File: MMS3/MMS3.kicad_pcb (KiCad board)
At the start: 2 copper layers, 100 x 50 mm, 162 parts, among them J1 86093488324755V1LF, J1 Chainbus in, J2 AMASS XT60, J2 Chainbus Out, J3 Programming header, J7 AMASS XT60, J8 RJ45_LED_Shielded, J800 USB_C_Receptacle_USB2.0_16P, J9 RJ45_LED_Shielded, Q700 MMST3904, SW1 BOOT, SW2 RESET, U1 STM32F405RGTx, U302 CH334P, U4 TPD2EUSB30DRTR-TP, U401 TPD2EUSB30DRTR-TP, U5 TPD2EUSB30DRTR-TP, U500 TJA1044GTK_3Z, U501 TJA1044GTK_3Z, U6 AT24C256C, U700 STM32F103CBTx, U801 FSUSB42UMX, U802 FSUSB42UMX, X1 X32258MOB4SI, X2 Q13FC1350000400, Y700 Crystal_GND24, Y900 Crystal_GND24

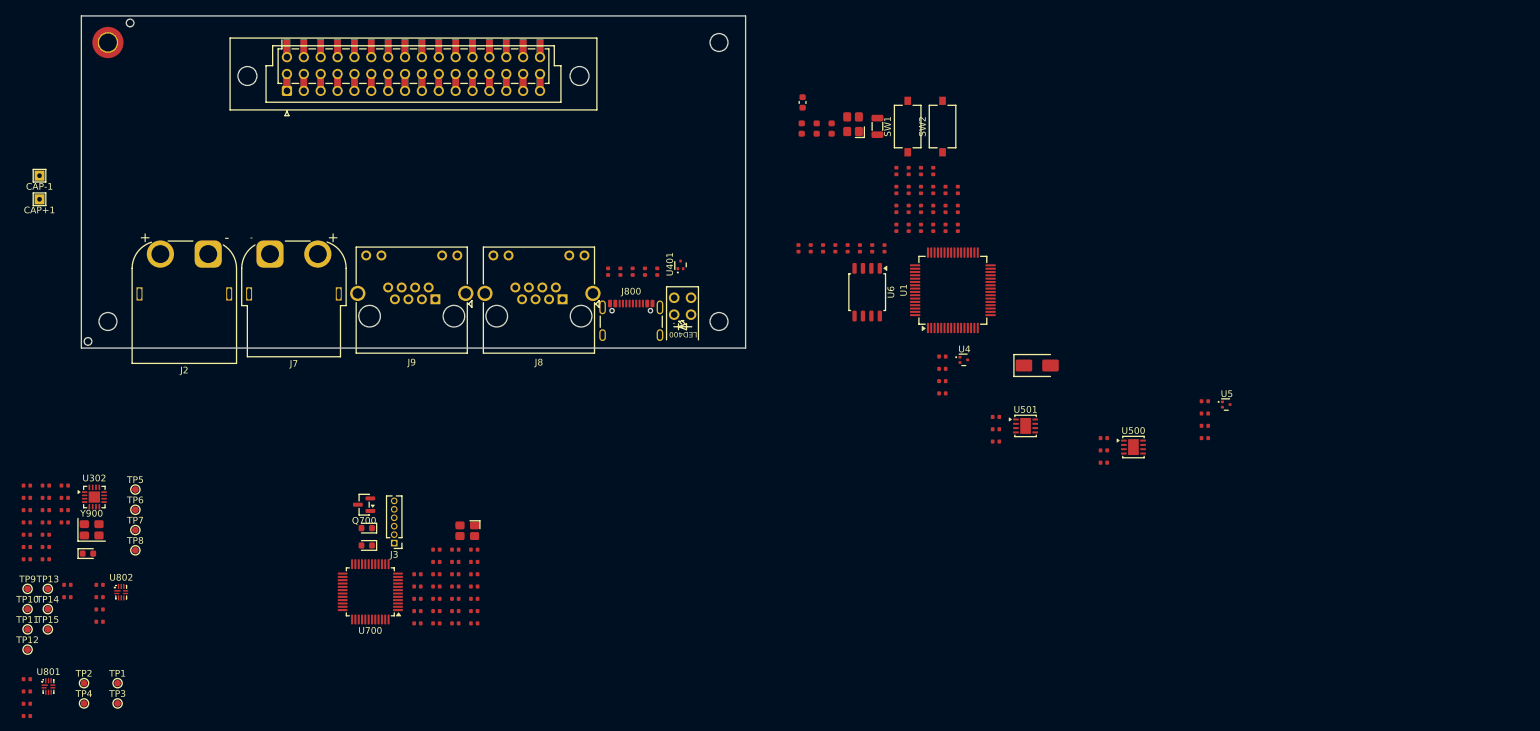
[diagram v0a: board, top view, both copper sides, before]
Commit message: schematic + partly layout
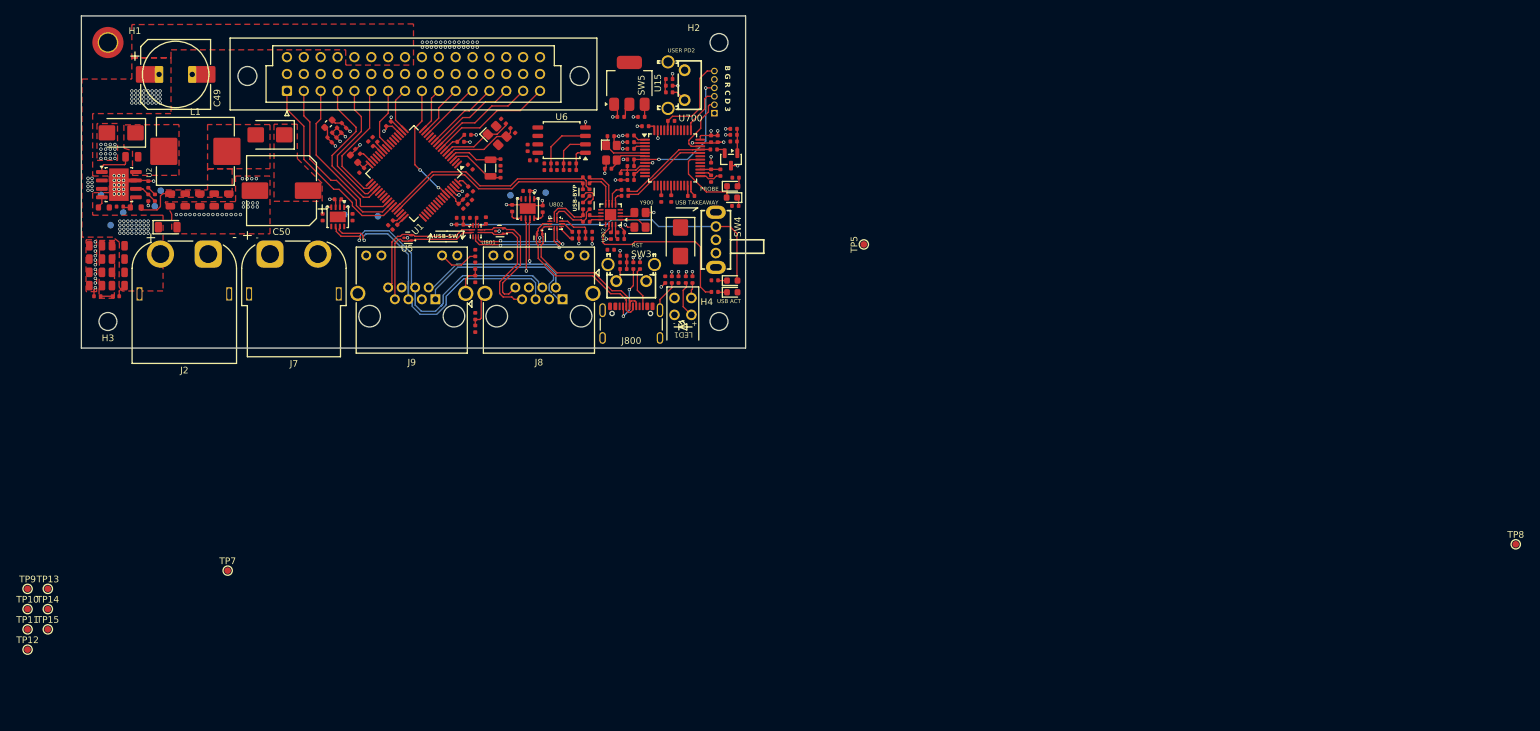
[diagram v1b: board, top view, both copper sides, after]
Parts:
- removed C14: 10uF, PCM_JLCPCB:C_0603
- removed C707, C708: 33pF, PCM_JLCPCB:C_0402
- removed CAP+1: Capacitor +, TestPoint:TestPoint_THTPad_1.5x1.5mm_Drill0.7mm
- removed CAP-1: Capacitor -, TestPoint:TestPoint_THTPad_1.5x1.5mm_Drill0.7mm
- removed H7, H9: ~, PCM_JLCPCB:Hole_Tooling_JLCPCB
- removed the J1 at (149.0, 89.5)
- removed the J2 at (149.0, 89.6)
- removed LED400: FixLed307, FixLed307:FixLed307
- removed R32: 22Ω, PCM_JLCPCB:R_0402
- removed SW1: BOOT, Button_Switch_SMD:SW_Tactile_SPST_NO_Straight_CK_PTS636Sx25SMTRLFS
- removed SW2: RESET, Button_Switch_SMD:SW_Tactile_SPST_NO_Straight_CK_PTS636Sx25SMTRLFS
- removed TP6: TestPoint, TestPoint:TestPoint_Pad_D1.0mm
- added C30: 10uF, PCM_JLCPCB:C_0805, F.Cu at (104.5, 118.6)
- added C31: 10uF, PCM_JLCPCB:C_0805, F.Cu at (101.2, 120.6)
- added C32: 10uF, PCM_JLCPCB:C_0805, F.Cu at (104.5, 120.6)
- added C33: 10uF, PCM_JLCPCB:C_0805, F.Cu at (101.2, 122.6)
- added C34: 10uF, PCM_JLCPCB:C_0805, F.Cu at (104.5, 122.6)
- added C35: 10uF, PCM_JLCPCB:C_0805, F.Cu at (101.2, 116.6)
- added C36: 10uF, PCM_JLCPCB:C_0402, F.Cu at (137.8, 98.5)
- added C37: 10uF, PCM_JLCPCB:C_0402, F.Cu at (137.1, 100.7)
- added C38: 220nF, PCM_JLCPCB:C_0805, F.Cu at (104.5, 116.6)
- added C39: 220nF, PCM_JLCPCB:C_0805, F.Cu at (101.2, 118.6)
- added C40: 100nF, PCM_JLCPCB:C_0805, F.Cu at (106.6, 103.2)
- added C41: 22uF, PCM_JLCPCB:C_0805, F.Cu at (112.4, 109.7)
- added C42: 22uF, PCM_JLCPCB:C_0805, F.Cu at (119.0, 109.7)
- added C43: 47pF, PCM_JLCPCB:C_0402, F.Cu at (109.1, 109.4)
- added C44: 4.7nF, PCM_JLCPCB:C_0402, F.Cu at (109.1, 107.4)
- added C45: 22uF, PCM_JLCPCB:C_0805, F.Cu at (116.8, 109.7)
- added C46: 22uF, PCM_JLCPCB:C_0805, F.Cu at (114.6, 109.7)
- added C47: 22uF, PCM_JLCPCB:C_0805, F.Cu at (121.2, 109.7)
- added C49: 100uF, Capacitor_SMD:CP_Elec_10x10, F.Cu at (113.2, 90.8)
- added C50: 100uF, Capacitor_SMD:CP_Elec_10x10, F.Cu at (129.1, 108.3)
- added C69: 100nF, PCM_JLCPCB:C_0402, F.Cu at (180.2, 97.2)
- added C74: 100nF, PCM_JLCPCB:C_0402, F.Cu at (183.3, 97.2)
- added D1: SMF58CA, PCM_JLCPCB:D_SOD-123FL, F.Cu at (112.0, 113.8)
- added D3: SS510B, PCM_JLCPCB:D_SMB, F.Cu at (105.0, 99.6)
- added D4: SS510B, PCM_JLCPCB:D_SMB, F.Cu at (127.4, 99.9)
- added D5: SS510B, PCM_JLCPCB:D_SMB, F.Cu at (189.2, 116.0)
- added L1: YSPI1050-100M, Inductor_SMD:L_Sunlord_MWSA1005S, F.Cu at (116.2, 102.4)
- added LED1: FixLed307, FixLed307:FixLed307, F.Cu at (189.5, 127.0)
- added R33: 24.9kΩ, PCM_JLCPCB:R_0402, F.Cu at (104.2, 124.2)
- added R34: 24.9kΩ, PCM_JLCPCB:R_0402, F.Cu at (101.4, 124.2)
- added R36: 43kΩ, PCM_JLCPCB:R_0603, F.Cu at (107.2, 110.8)
- added R37: 8.2kΩ, PCM_JLCPCB:R_0402, F.Cu at (104.8, 110.7)
- added R38: 12kΩ, PCM_JLCPCB:R_0402, F.Cu at (110.1, 109.4)
- added R39: 240kΩ, PCM_JLCPCB:R_0603, F.Cu at (102.4, 110.8)
- added R40: 1kΩ, PCM_JLCPCB:R_0402, F.Cu at (190.0, 121.7)
- added SW3: TC-6615Z-12.5-260, Tact-sw:SW-TH_4P-L7.3-TC-6615Z-12.5-260, F.Cu at (181.8, 120.7)
- added SW4: SK12D07VG5, Slide-SW:SW-TH_SK12D07VG5-1, F.Cu at (194.5, 115.7)
- added SW5: TC-6615Z-12.5-260, Tact-sw:SW-TH_4P-L7.3-TC-6615Z-12.5-260, F.Cu at (188.6, 92.4)
- added TP16: TestPoint, TestPoint:TestPoint_Pad_D1.0mm, B.Cu at (103.4, 113.5)
- added TP17: TestPoint, TestPoint:TestPoint_Pad_D1.0mm, B.Cu at (110.0, 110.7)
- added TP18: TestPoint, TestPoint:TestPoint_Pad_D1.0mm, B.Cu at (105.3, 111.6)
- added TP19: TestPoint, TestPoint:TestPoint_Pad_D1.0mm, B.Cu at (111.0, 108.3)
- added TP20: TestPoint, TestPoint:TestPoint_Pad_D1.0mm, B.Cu at (102.0, 109.0)
- added U15: AMS1117-3.3, Package_TO_SOT_SMD:SOT-223-3_TabPin2, F.Cu at (181.5, 92.2)
- added U2: TPS54560BDDA, Package_SO:Texas_R-PDSO-G8_EP2.95x4.9mm_Mask2.4x3.1mm_ThermalVias, F.Cu at (104.7, 107.4)
- C12: value 10uF -> 100nF; footprint PCM_JLCPCB:C_0603 -> PCM_JLCPCB:C_0402
- D6: value SS34 -> Red; footprint PCM_JLCPCB:D_SMA -> PCM_JLCPCB:D_0603
- J3, TP1, TP2, TP3, TP4: moved to B.Cu
- R22: value 22Ω -> 100Ω
- R27, R31: value 22Ω -> 1kΩ
- moved TP8 207.8 mm to (314.9, 161.5)
- moved R4 132.6 mm to (142.5, 101.2), turned to -45 degrees
- moved U5 125.8 mm to (148.1, 115.4), turned to 180 degrees
- moved TP5 115.7 mm to (216.8, 116.4), turned to 90 degrees
- moved R6 112.9 mm to (158.3, 119.6), turned to 90 degrees
- moved R2 112.5 mm to (158.3, 117.7), turned to 90 degrees
- moved C2 111.4 mm to (158.3, 121.6), turned to -90 degrees
- moved R308 108.4 mm to (194.3, 123.5)
- moved U501 108.2 mm to (137.6, 112.2), turned to -90 degrees
- moved R31 107.7 mm to (194.3, 121.8), turned to 180 degrees
- moved C28 106.1 mm to (178.7, 100.1)
- moved C4 105.7 mm to (135.3, 112.3), turned to 90 degrees
- moved C6 104.9 mm to (137.6, 109.6), turned to 180 degrees
- moved D301 104.7 mm to (197.0, 123.6)
- moved R27 104.0 mm to (191.0, 121.7), turned to -90 degrees
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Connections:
- net Net-(R18-Pad1) renamed /USB HUB/USBBYP.D+
- C12 pad 1: +3V3 -> Net-(U1-NRST)
- D6 pad 1: +5V -> Net-(D6-Pad1)
- D6 pad 2: VBUS -> /Slide-SW/SEL
- J1 pad a1: (no net) -> /Interboard_connector/Altmode3
- J1 pad a10: (no net) -> /Interboard_connector/Altmode9
- J1 pad a11: (no net) -> /Interboard_connector/Altmode8
- J1 pad a12: (no net) -> /Interboard_connector/Altmode7
- J1 pad a13: (no net) -> /Interboard_connector/Altmode15
- J1 pad a14: (no net) -> /Interboard_connector/Altmode14
- J1 pad a15: (no net) -> /Interboard_connector/Altmode13
- J1 pad a16: (no net) -> /Interboard_connector/Altmode12
- J1 pad a2: (no net) -> /Interboard_connector/Altmode2
- J1 pad a3: (no net) -> /Interboard_connector/Altmode1
- J1 pad a4: (no net) -> /Interboard_connector/Altmode6
- J1 pad a5: (no net) -> /Interboard_connector/Altmode5
- J1 pad a6: (no net) -> /Interboard_connector/Altmode4
- J1 pad a7: (no net) -> /Interboard_connector/Altmode16
- J1 pad a8: (no net) -> /Interboard_connector/Altmode10
- J1 pad a9: (no net) -> /Interboard_connector/Altmode11
- J1 pad b1: (no net) -> /Interboard_connector/Chainbus_UART_addr0
- J1 pad b10: (no net) -> /I2C_Flash/I2C_Memory.SCL
- J1 pad b11: (no net) -> /Interboard_connector/Chainbus_I2C_addr2
- J1 pad b12: (no net) -> /Interboard_connector/Chainbus.SCK
- J1 pad b13: (no net) -> /Interboard_connector/Chainbus.MOSI
- J1 pad b14: (no net) -> /Interboard_connector/Chainbus.MISO
- J1 pad b15: (no net) -> /Interboard_connector/Chainbus.RX
- J1 pad b16: (no net) -> /Interboard_connector/Chainbus.TX
- J1 pad b2: (no net) -> /Interboard_connector/Chainbus_UART_addr1
- J1 pad b3: (no net) -> /Interboard_connector/Chainbus_UART_addr2
- J1 pad b4: (no net) -> /Interboard_connector/Chainbus_I2C_addr0
- J1 pad b5: (no net) -> /Interboard_connector/Chainbus_I2C_addr1
- J1 pad b6: (no net) -> /Interboard_connector/Chainbus_SPI_CS0
- J1 pad b7: (no net) -> /Interboard_connector/Chainbus_SPI_CS1
- J1 pad b8: (no net) -> /Interboard_connector/Chainbus_SPI_CS2
- J1 pad b9: (no net) -> /I2C_Flash/I2C_Memory.SDA
- J1 pad c1: (no net) -> GND
- J1 pad c10: (no net) -> GND
- J1 pad c11: (no net) -> GND
- J1 pad c12: (no net) -> GND
- J1 pad c13: (no net) -> unconnected-(J1-Padc13)
- J1 pad c14: (no net) -> unconnected-(J1-Padc14)
- J1 pad c15: (no net) -> +12V stby
- J1 pad c16: (no net) -> GND
- J1 pad c2: (no net) -> +5V
- J1 pad c3: (no net) -> +5V
- J1 pad c4: (no net) -> GND
- J1 pad c5: (no net) -> BRD_VIN
- J1 pad c6: (no net) -> BRD_VIN
- J1 pad c7: (no net) -> BRD_VIN
- J1 pad c8: (no net) -> BRD_VIN
- J1 pad c9: (no net) -> GND
- J2 pad 1: GNDPWR -> GND
- J7 pad 1: GNDPWR -> GND
- J8 pad 1: /MMS_CONNECTOR_DOWNSTREAM/CAN1.- -> /CAN_TR1/CAN.-
- J8 pad 2: /MMS_CONNECTOR_DOWNSTREAM/CAN1.+ -> /CAN_TR1/CAN.+
- J8 pad 4: /MMS_CONNECTOR_DOWNSTREAM/CAN2.- -> /CAN_TR2/CAN.-
- J8 pad 5: /MMS_CONNECTOR_DOWNSTREAM/CAN2.+ -> /CAN_TR2/CAN.+
- J8 pad 6: +12V -> +12V stby
- J800 pad A6: /USBC_CONN/USBC_CONN.D+ -> /USB switch1/USB_OUT2.D+
- J800 pad A7: /USBC_CONN/USBC_CONN.D- -> /USB switch1/USB_OUT2.D-
- J800 pad B6: /USBC_CONN/USBC_CONN.D+ -> /USB switch1/USB_OUT2.D+
- J800 pad B7: /USBC_CONN/USBC_CONN.D- -> /USB switch1/USB_OUT2.D-
- J800 pad SH: (no net) -> Net-(J800-SHIELD)
- J9 pad 1: /MMS_CONNECTOR_UPSTREAM/CAN1.- -> /CAN_TR1/CAN.-
- J9 pad 2: /MMS_CONNECTOR_UPSTREAM/CAN1.+ -> /CAN_TR1/CAN.+
- J9 pad 4: /MMS_CONNECTOR_UPSTREAM/CAN2.- -> /CAN_TR2/CAN.-
- J9 pad 5: /MMS_CONNECTOR_UPSTREAM/CAN2.+ -> /CAN_TR2/CAN.+
- J9 pad 6: +12V -> +12V stby
- R19 pad 1: Net-(R19-Pad1) -> /USB HUB/USBBYP.D-
- R20 pad 1: Net-(R19-Pad1) -> /USB HUB/USBBYP.D-
- R20 pad 2: /USB HUB/USBOUT1.D- -> /MCU/USB_MCU.D-
- R21 pad 2: /USB HUB/USBOUT1.D+ -> /MCU/USB_MCU.D+
- R22 pad 1: Net-(R22-Pad1) -> /MCU/NRST
- R22 pad 2: /USB HUB/USBOUT2.D- -> Net-(U1-NRST)
- R27 pad 1: Net-(R27-Pad1) -> /MCU/USER_LED_3
- R27 pad 2: /USB HUB/USBOUT2.D+ -> Net-(LED1-Pad3)
- R31 pad 1: Net-(R19-Pad1) -> Net-(D6-Pad1)
- R31 pad 2: Net-(R22-Pad1) -> GND
- R704 pad 2: /STlink-BMprobe/SWD.SWCLK -> /MCU/SWD.SWCLK
- R708 pad 1: /STlink-BMprobe/SWD.~{RST} -> /MCU/SWD.~{RST}
- R715 pad 1: /STlink-BMprobe/SWD.SWCLK -> /MCU/SWD.SWCLK
- R716 pad 1: /STlink-BMprobe/SWD.SWDIO -> /MCU/SWD.SWDIO
- R802 pad 1: /USB switch/SEL -> /Slide-SW/SEL
- R902 pad 1: /USB HUB/USBOUT2.D- -> /STlink-BMprobe/ST-LINK.D-
- R903 pad 1: /USB HUB/USBOUT2.D+ -> /STlink-BMprobe/ST-LINK.D+
- R906 pad 1: /USB HUB/USBOUT1.D- -> /MCU/USB_MCU.D-
- R907 pad 1: /USB HUB/USBOUT1.D+ -> /MCU/USB_MCU.D+
- TP10 pad 1: /STlink-BMprobe/SWD.SWCLK -> /MCU/SWD.SWCLK
- TP11 pad 1: /STlink-BMprobe/SWD.~{RST} -> /MCU/SWD.~{RST}
- TP9 pad 1: /STlink-BMprobe/SWD.SWDIO -> /MCU/SWD.SWDIO
- U1 pad 20: unconnected-(U1-PA4-Pad20) -> /MCU/BOOT_EN
- U1 pad 25: /I2C_Flash/A0 -> /MCU/USER_LED_3
- U1 pad 29: /MCU/Chainbus.SCL -> /I2C_Flash/I2C_Memory.SCL
- U1 pad 30: /MCU/Chainbus.SDA -> /I2C_Flash/I2C_Memory.SDA
- U1 pad 51: /MCU/Chainbus.TX -> /Interboard_connector/Chainbus.TX
- U1 pad 52: /MCU/Chainbus.RX -> /Interboard_connector/Chainbus.RX
- U1 pad 53: /MCU/Chainbus.MOSI -> /Interboard_connector/Chainbus.MOSI
- U1 pad 55: /MCU/Chainbus.SCK -> /Interboard_connector/Chainbus.SCK
- U1 pad 56: /MCU/Chainbus.MISO -> /Interboard_connector/Chainbus.MISO
- U1 pad 7: /MCU/NRST -> Net-(U1-NRST)
- U401 pad 1: /USBC_CONN/USBC_CONN.D+ -> /USB switch1/USB_OUT2.D+
- U401 pad 2: /USBC_CONN/USBC_CONN.D- -> /USB switch1/USB_OUT2.D-
- U801 pad 1: /USB switch/USB_IN.D+ -> /MMS_CONNECTOR_UPSTREAM/USB_MMS_CONN.D+
- U801 pad 2: /USB switch/USB_IN.D- -> /MMS_CONNECTOR_UPSTREAM/USB_MMS_CONN.D-
- U801 pad 6: /USB switch/USB_OUT1.D- -> /MMS_CONNECTOR_DOWNSTREAM/USB_MMS_CONN.D-
- U801 pad 7: /USB switch/USB_OUT1.D+ -> /MMS_CONNECTOR_DOWNSTREAM/USB_MMS_CONN.D+
- U802 pad 1: /USB switch1/USB_IN.D+ -> /USB HUB/USBIN1.D+
- U802 pad 2: /USB switch1/USB_IN.D- -> /USB HUB/USBIN1.D-
- U802 pad 6: /USB switch1/USB_OUT1.D- -> /USB switch/USB_OUT2.D-
- U802 pad 7: /USB switch1/USB_OUT1.D+ -> /USB switch/USB_OUT2.D+
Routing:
- net GND: track 0.00 -> 70.8 mm, vias 0 -> 139
- net /Slide-SW/SEL: track 0.00 -> 51.7 mm, vias 0 -> 1
- net /CAN_TR2/CAN.+: track 0.00 -> 49.7 mm, vias 0 -> 1
- net /CAN_TR2/CAN.-: track 0.00 -> 47.0 mm, vias 0 -> 1
- net +3V3: track 0.00 -> 39.0 mm, vias 0 -> 7
- net /CAN_TR1/CAN.-: track 0.00 -> 34.4 mm, vias 0 -> 1
- net /MCU/USB_MCU.D+: track 0.00 -> 32.4 mm
- net /MCU/USB_MCU.D-: track 0.00 -> 31.9 mm
- net /CAN_TR1/CAN.+: track 0.00 -> 30.3 mm, vias 0 -> 1
- net /Interboard_connector/Altmode3: track 0.00 -> 29.2 mm
- net /Interboard_connector/Altmode2: track 0.00 -> 27.1 mm
- net Net-(U302-PGANG): track 0.00 -> 26.4 mm
- net /USB switch1/USB_OUT2.D-: track 0.00 -> 26.0 mm
- net /USB switch1/USB_OUT2.D+: track 0.00 -> 25.3 mm
- net /Interboard_connector/Altmode1: track 0.00 -> 24.9 mm
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- added copper zone on F.Cu, net +5V
- added copper zone on F.Cu, net /VRM/Cap_protec
- added copper zone on F.Cu, net BRD_VIN
- added copper zone on F.Cu, net GND
- added copper zone on F.Cu, net Net-(C41-Pad1)
- added copper zone on F.Cu, net Net-(U2-SW)
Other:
- board text added: "B G R C D 3"
- board text added: "LINK PRG"
- board text added: "PROBE"
- board text added: "RST"
- board text added: "USB ACT"
- board text added: "USB TAKEAWAY"
- board text added: "USB-BYP"
- board text added: "USB-SW"
- board text added: "USER PD2"

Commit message: almost done
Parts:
- removed TP15: TestPoint, TestPoint:TestPoint_Pad_D1.0mm
- TP10, TP11, TP12, TP13, TP14, TP5, TP7, TP8, TP9: moved to B.Cu
- moved TP8 150.7 mm to (181.4, 91.8), turned to 180 degrees
- moved TP12 123.6 mm to (189.8, 103.2), turned to 180 degrees
- moved TP9 121.7 mm to (193.8, 103.2), turned to 180 degrees
- moved TP10 121.0 mm to (193.8, 107.6), turned to 180 degrees
- moved TP14 118.8 mm to (189.4, 100.6), turned to 180 degrees
- moved TP11 117.9 mm to (189.4, 109.6), turned to 180 degrees
- moved TP13 114.6 mm to (187.6, 102.2), turned to 180 degrees
- moved TP7 68.7 mm to (160.6, 109.4), turned to 180 degrees
- moved TP5 46.1 mm to (175.6, 95.8)
- moved TP1 7.60 mm to (161.8, 111.3)
- moved TP18 3.80 mm to (108.4, 109.4)
- moved TP4 3.62 mm to (139.0, 108.3)
- moved TP19 0.74 mm to (111.2, 109.0)
- moved TP2 0.60 mm to (143.1, 112.4)
- moved TP3 0.41 mm to (163.5, 108.6)
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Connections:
- net /Interboard_connector/Chainbus_SPI_CS0 renamed /Interboard_connector/Chainbus_addr5
- net /Interboard_connector/Chainbus_SPI_CS1 renamed /Interboard_connector/Chainbus_addr6
- net /Interboard_connector/Chainbus_SPI_CS2 renamed /Interboard_connector/Chainbus_addr7
- J1 pad b1: /Interboard_connector/Chainbus_UART_addr0 -> /Interboard_connector/Chainbus_addr3
- J1 pad b11: /Interboard_connector/Chainbus_I2C_addr2 -> /Interboard_connector/Chainbus.CS
- J1 pad b2: /Interboard_connector/Chainbus_UART_addr1 -> /Interboard_connector/Chainbus_addr4
- J1 pad b3: /Interboard_connector/Chainbus_UART_addr2 -> /Interboard_connector/Chainbus_addr0
- J1 pad b4: /Interboard_connector/Chainbus_I2C_addr0 -> /Interboard_connector/Chainbus_addr1
- J1 pad b5: /Interboard_connector/Chainbus_I2C_addr1 -> /Interboard_connector/Chainbus_addr2
- U1 pad 21: /Interboard_connector/Chainbus_UART_addr2 -> /Interboard_connector/Chainbus_addr2
- U1 pad 22: /Interboard_connector/Chainbus_UART_addr0 -> /Interboard_connector/Chainbus_addr1
- U1 pad 23: /Interboard_connector/Chainbus_UART_addr1 -> /Interboard_connector/Chainbus_addr0
- U1 pad 40: /Interboard_connector/Chainbus_I2C_addr2 -> /Interboard_connector/Chainbus_addr3
- U1 pad 50: /Interboard_connector/Chainbus_I2C_addr0 -> /Interboard_connector/Chainbus.CS
- U1 pad 57: /Interboard_connector/Chainbus_I2C_addr1 -> /Interboard_connector/Chainbus_addr4
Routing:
- net +3V3: track 39.0 -> 309.6 mm, vias 7 -> 49
- net +12V stby: track 0.00 -> 151.0 mm
- net +5V: track 5.87 -> 116.9 mm, vias 2 -> 25
- net Net-(J8-~-Pad10): track 0.00 -> 74.0 mm, vias 0 -> 5
- net /MCU/USER_LED_3: track 0.70 -> 73.4 mm, vias 1 -> 7
- net /MCU/SWD.SWDIO: track 0.90 -> 58.0 mm, vias 1 -> 2
- net /MCU/SWD.SWCLK: track 0.00 -> 54.6 mm, vias 0 -> 4
- net /I2C_Flash/I2C_Memory.SCL: track 0.00 -> 53.7 mm, vias 0 -> 1
- net /MCU/NRST: track 2.92 -> 56.0 mm, vias 1 -> 4
- net /I2C_Flash/I2C_Memory.SDA: track 0.00 -> 49.3 mm, vias 0 -> 1
- net /MCU/USR_BUTTON: track 2.30 -> 51.4 mm, vias 0 -> 1
- net /Interboard_connector/Chainbus.SCK: track 0.00 -> 49.0 mm, vias 0 -> 1
- net /Interboard_connector/Chainbus.MISO: track 0.00 -> 39.8 mm, vias 0 -> 1
- net GND: track 70.8 -> 108.1 mm, vias 139 -> 249
- net /Interboard_connector/Chainbus_addr4: track 0.00 -> 34.8 mm, vias 0 -> 1
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- added copper zone on F.Cu, net +3V3
- added copper zone on In2.Cu, net +3V3
- added copper zone on In2.Cu, net +5V
- added copper zone on In2.Cu, net /MCU/VDDA
- added copper zone on In1.Cu, net GND
- added copper zone on F.Cu, net VBUS
- added copper zone on In2.Cu, net VBUS
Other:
- copper layers 2 -> 4

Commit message: prod ready
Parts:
- added G***: LOGO, LOGO, F.Cu at (149.2, 106.1)
- added G***: LOGO, LOGO, F.Cu at (141.4, 109.9)
- added G***: LOGO, LOGO, B.Cu at (131.0, 97.5)
- added G***: LOGO, LOGO, B.Cu at (133.3, 102.7)
- added G***: LOGO, LOGO, B.Cu at (153.3, 111.0)
- added REF**: WEEE-Logo_4.2x6mm_SilkScreen, Symbol:WEEE-Logo_4.2x6mm_SilkScreen, B.Cu at (118.2, 98.3)
- moved TP20 3.33 mm to (104.4, 111.2)
- moved TP8 3.31 mm to (184.0, 89.8)
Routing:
- net Net-(C1-Pad1): track 5.84 -> 27.5 mm
- net Net-(C2-Pad1): track 4.79 -> 23.9 mm
- net Net-(J800-SHIELD): track 4.94 -> 22.9 mm
- net +5V: track 116.9 -> 108.2 mm, vias 25 -> 24
- net +3V3: track 309.6 -> 318.1 mm
- net GND: track 108.1 -> 114.5 mm, vias 249 -> 370
- net /MMS_CONNECTOR_DOWNSTREAM/USB_MMS_CONN.D+: track 18.7 -> 15.2 mm
- net Net-(U2-RT/CLK): track 1.75 -> 4.74 mm, vias 0 -> 1
- net /CAN_TR2/CAN.+: track 49.7 -> 47.5 mm
- net /MMS_CONNECTOR_DOWNSTREAM/USB_MMS_CONN.D-: track 19.5 -> 17.4 mm
- net Net-(U6-WP): track 0.00 -> 1.54 mm
- net /CAN_TR1/CAN.+: track 30.3 -> 31.8 mm
- net /MCU/VDDA: track 4.88 -> 6.27 mm
- net /STlink-BMprobe/ST-LINK.D+: track 15.3 -> 16.4 mm
- net +12V stby: track 151.0 -> 152.1 mm
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- added copper zone on B.Cu, net +3V3
- added copper zone on B.Cu, net BRD_VIN
- added copper zone on B.Cu, net GND
- added copper zone on In2.Cu, net GND
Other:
- board text added: "0 1"
- board text added: "12V"
- board text added: "A2 A1 A0"
- board text added: "AH2026"
- board text added: "CAN1"
- board text added: "CAN1+"
- board text added: "CAN1-"
- board text added: "CAN2"
- board text added: "CAN2+"
- board text added: "CAN2-"
- board text added: "ChainBus"
- board text added: "DESIGNED IN POLAND"
- board text added: "FW"
- board text added: "GND"
- board text added: "HUB"
- board text added: "MODULAR MECHANICA MMS3 ARTEM.H. :) 2026"
- board text added: "QC"
- board text added: "REV"
- board text added: "S / N"
- board text added: "SWITCH"
- board text added: "USB+"
- board text added: "USB-"
- board text added: "XA1"
- board text added: "arthorh.github.io/ChainBus"
- board text added: "connector powered by"
- board text added: "i"

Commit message: prod
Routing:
- net /I2C_Flash/A0: track 2.86 -> 3.86 mm
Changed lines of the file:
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@@
 			(plot_on_all_layers_selection 0x00000000_00000000_00000000_00000000)
 			(disableapertmacros no)
-			(usegerberextensions no)
+			(usegerberextensions yes)
 			(usegerberattributes yes)
 			(usegerberadvancedattributes yes)
@@
 			(sketchdnponfab yes)
 			(crossoutdnponfab yes)
-			(subtractmaskfromsilk no)
+			(subtractmaskfromsilk yes)
 			(outputformat 1)
 			(mirror no)
-			(drillshape 1)
+			(drillshape 0)
 			(scaleselection 1)
-			(outputdirectory "")
+			(outputdirectory "jlcpcb/gerber/")
 		)
 	)
@@
 			)
 		)
+		(property "LCSC" "C1850354"
+			(at 0 0 0)
+			(layer "F.SilkS")
+			(hide yes)
+			(effects
+				(font
+					(size 1.27 1.27)
+					(thickness 0.15)
+				)
+			)
+		)
 		(property ki_fp_filters "Texas*R*PDSO*G8*")
 		(sheetname "/VRM/")
@@
 			)
 		)
-		(attr through_hole)
+		(attr through_hole exclude_from_pos_files exclude_from_bom)
 		(duplicate_pad_numbers_are_jumpers no)
 		(fp_line
@@
 			)
 		)
+		(property "LCSC" "C6186"
+			(at 0.15 -0.1 0)
+			(layer "F.SilkS")
+			(hide yes)
+			(effects
+				(font
+					(size 1.27 1.27)
+					(thickness 0.15)
+				)
+			)
+		)
 		(property ki_fp_filters "SOT?223*TabPin2*")
 		(sheetname "/VRM/")
@@
 			)
 		)
+		(property "LCSC" "C5373042"
+			(at 0 0 0)
+			(layer "F.SilkS")
+			(hide yes)
+			(effects
+				(font
+					(size 1.27 1.27)
+					(thickness 0.15)
+				)
+			)
+		)
 		(sheetname "/USB HUB/")
 		(sheetfile "USB HUB.kicad_sch")
@@
 			)
 		)
+		(attr exclude_from_bom)
 		(duplicate_pad_numbers_are_jumpers no)
 		(fp_circle
@@
 			)
 		)
+		(attr exclude_from_bom)
 		(duplicate_pad_numbers_are_jumpers no)
 		(fp_circle
@@
 			)
 		)
+		(attr exclude_from_bom)
 		(duplicate_pad_numbers_are_jumpers no)
 		(fp_circle
@@
 			)
 		)
+		(attr exclude_from_bom)
 		(duplicate_pad_numbers_are_jumpers no)
 		(fp_circle
@@
 			)
 		)
+		(attr exclude_from_bom)
 		(duplicate_pad_numbers_are_jumpers no)
 		(fp_circle
@@
 			)
 		)
+		(attr exclude_from_bom)
 		(duplicate_pad_numbers_are_jumpers no)
 		(fp_circle
@@
 			)
 		)
+		(attr exclude_from_bom)
 		(duplicate_pad_numbers_are_jumpers no)
 		(fp_circle
@@
 			)
 		)
+		(attr exclude_from_bom)
 		(duplicate_pad_numbers_are_jumpers no)
 		(fp_circle
@@
 			)
 		)
+		(attr exclude_from_bom)
 		(duplicate_pad_numbers_are_jumpers no)
 		(fp_circle
@@
 			)
 		)
+		(attr exclude_from_bom)
 		(duplicate_pad_numbers_are_jumpers no)
 		(fp_circle
@@
 			)
 		)
+		(attr exclude_from_bom)
 		(duplicate_pad_numbers_are_jumpers no)
 		(fp_circle
@@
 			)
 		)
+		(attr exclude_from_bom)
 		(duplicate_pad_numbers_are_jumpers no)
 		(fp_circle
@@
 			)
 		)
+		(attr exclude_from_bom)
 		(duplicate_pad_numbers_are_jumpers no)
 		(fp_circle
@@
 			)
 		)
+		(attr exclude_from_bom)
 		(duplicate_pad_numbers_are_jumpers no)
 		(fp_circle
@@
 			)
 		)
+		(attr exclude_from_bom)
 		(duplicate_pad_numbers_are_jumpers no)
 		(fp_circle
@@
 			)
 		)
+		(attr exclude_from_bom)
 		(duplicate_pad_numbers_are_jumpers no)
 		(fp_circle
@@
 			)
 		)
+		(attr exclude_from_bom)
 		(duplicate_pad_numbers_are_jumpers no)
 		(fp_circle
@@
 			)
 		)
+		(attr exclude_from_bom)
 		(duplicate_pad_numbers_are_jumpers no)
 		(fp_circle
@@
 		(width 0.2)
 		(layer "F.Cu")
+		(net "/I2C_Flash/A0")
+	)
+	(segment
+		(start 173.5 104.2)
+		(end 173.5 105.2)
+		(width 0.2)
+		(layer "F.Cu")
